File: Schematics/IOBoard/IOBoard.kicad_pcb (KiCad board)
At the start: 2 copper layers, 46.9 x 12.1 mm, 8 parts, among them J1 OLED, J2 Mainboard, J3 Main_output, U1 ATSAMD21E18A-M

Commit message: IOBoard completed
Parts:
- removed C/D: SW(C/D), Connector_PinHeader_2.54mm:PinHeader_1x02_P2.54mm_Vertical
- removed R6: 10k, Resistor_SMD:R_0603_1608Metric
- added C2: 10uF, Capacitor_SMD:C_0603_1608Metric, F.Cu at (111.4, 67.7)
- added J4: MainBoard, Connector_PinSocket_2.54mm:PinSocket_2x05_P2.54mm_Vertical_SMD, B.Cu at (114.3, 63.7)
- added JP1: D0, Jumper:SolderJumper-3_P1.3mm_Bridged12_Pad1.0x1.5mm, F.Cu at (105.8, 67.1)
- added JP2: D1, Jumper:SolderJumper-3_P1.3mm_Bridged12_Pad1.0x1.5mm, F.Cu at (108.5, 67.1)
- added JP3: D1, Jumper:SolderJumper-3_P1.3mm_Bridged12_Pad1.0x1.5mm, B.Cu at (129.8, 60.6)
- added R2: 10k, Resistor_SMD:R_0603_1608Metric, F.Cu at (118.2, 60.3)
- J2: value Mainboard -> Prog; footprint Connector_PinHeader_2.54mm:PinHeader_2x06_P2.54mm_Vertical_SMD -> Connector:Tag-Connect_TC2030-IDC-NL_2x03_P1.27mm_Vertical
- moved J2 11.6 mm to (125.9, 63.7)
- moved C1 5.76 mm to (115.3, 59.4)
- turned U1 to 0 degrees
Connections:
- net /I2C_SDA_IN renamed /TX
- J1 pad 3: /I2C_SCL_OUT -> /OLED_SCL_I2C
- J1 pad 4: /I2C_SDA_OUT -> /OLED_SDA_I2C
- J2 pad 1: GND -> /SWD
- J2 pad 2: /SEL3 -> /SWC
- J2 pad 3: /SEL2 -> GND
- J2 pad 4: /SEL1 -> /RX
- J2 pad 5: GND -> +3V3
- J3 pad 1: /DAC/ADC/1-Wire -> /OUTPUT
- U1 pad 1: Net-(D1-Pad1) -> /OLED_SDA_I2C
- U1 pad 11: /I2C_SDA_OUT -> /D1_I2C
- U1 pad 12: /I2C_SCL_OUT -> /D0_I2C
- U1 pad 13: (no net) -> Net-(D1-Pad2)
- U1 pad 14: (no net) -> Net-(D1-Pad1)
- U1 pad 15: /SEL2 -> (no net)
- U1 pad 16: /SEL1 -> (no net)
- U1 pad 17: /SEL3 -> /TX/RX
- U1 pad 18: (no net) -> /SEL0
- U1 pad 19: (no net) -> /SEL1
- U1 pad 2: Net-(D1-Pad2) -> /OLED_SCL_I2C
- U1 pad 20: (no net) -> /SEL2
- U1 pad 22: /I2C_SCL_IN -> /RX
- U1 pad 23: /USB_D+ -> (no net)
- U1 pad 24: /USB_D- -> (no net)
- U1 pad 3: (no net) -> /DAC/ADC
- U1 pad 4: /DAC/ADC/1-Wire -> (no net)
- U1 pad 5: (no net) -> /D0_SPI
- U1 pad 6: (no net) -> /SCK
- U1 pad 7: (no net) -> /SS
- U1 pad 8: (no net) -> /D1_SPI
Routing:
- net /I2C_SDA_OUT: track 28.2 -> 0.00 mm
- net /DAC/ADC: track 0.00 -> 24.7 mm, vias 0 -> 1
- net /OLED_SCL_I2C: track 0.00 -> 24.7 mm
- net /DAC/ADC/1-Wire: track 22.3 -> 0.00 mm
- net /I2C_SCL_OUT: track 21.4 -> 0.00 mm
- net /OLED_SDA_I2C: track 0.00 -> 20.0 mm
- net /TX/RX: track 0.00 -> 19.9 mm, vias 0 -> 1
- net GND: track 36.6 -> 55.3 mm, vias 6 -> 5
- net /D0_I2C: track 0.00 -> 12.3 mm
- net /USB_D+: track 12.2 -> 0.00 mm, vias 1 -> 0
- net /SWD: track 11.5 -> 21.3 mm, vias 0 -> 1
- net /SWC: track 8.80 -> 17.8 mm, vias 0 -> 1
- net /RX: track 0.00 -> 8.78 mm, vias 0 -> 1
- net /D1_I2C: track 0.00 -> 8.70 mm
- net /D1: track 0.00 -> 7.76 mm, vias 0 -> 1
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
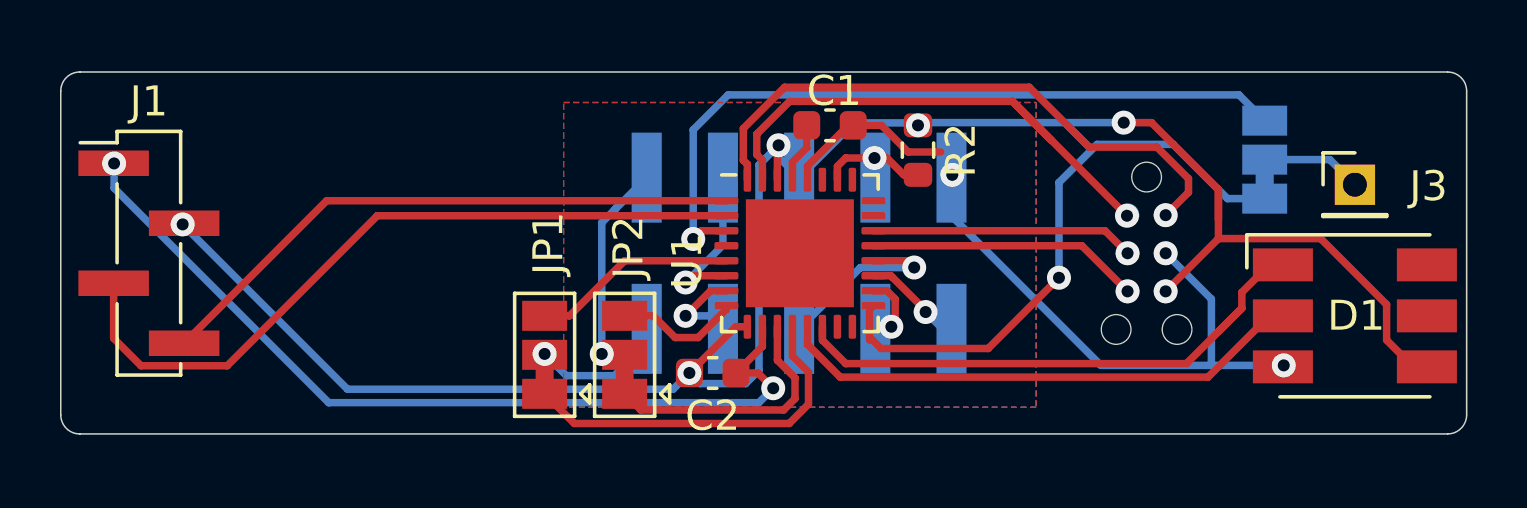
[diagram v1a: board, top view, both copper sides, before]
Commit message: Finished circuit - pre mousebites
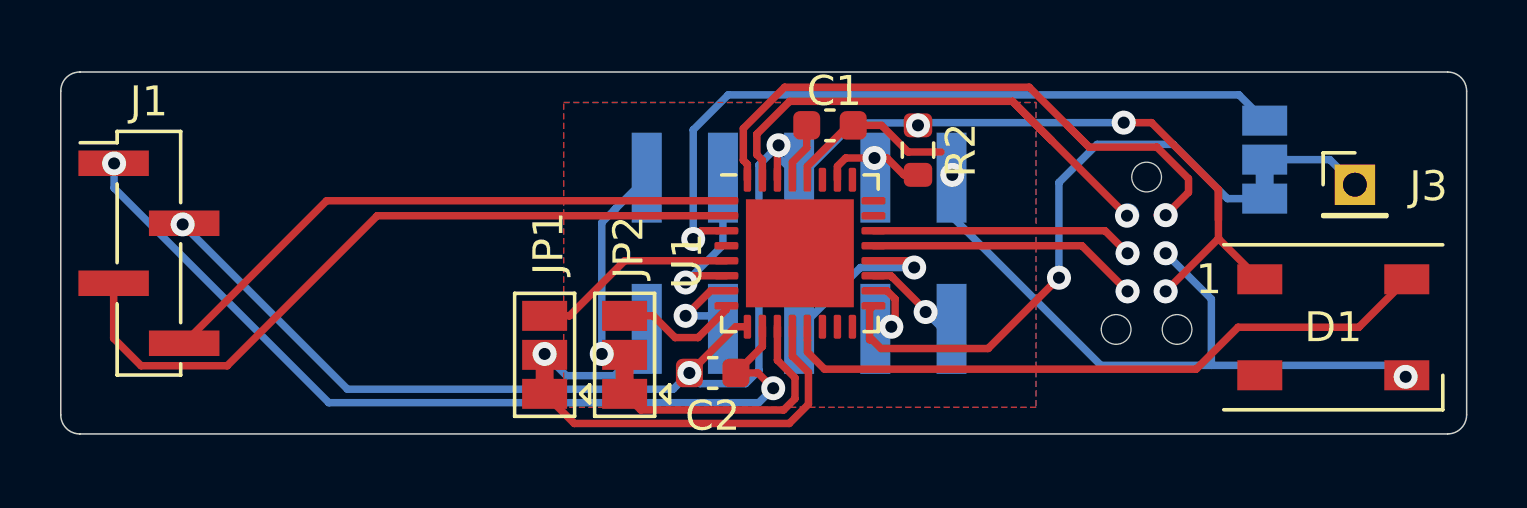
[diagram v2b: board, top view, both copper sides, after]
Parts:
- D1: value APA102 -> WS2812B; footprint LED_SMD:LED_RGB_5050-6 -> LED_SMD:LED_WS2812B_PLCC4_5.0x5.0mm_P3.2mm
- moved D1 0.81 mm to (132.1, 66.2)
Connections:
- D1 pad 1: Net-(D1-Pad1) -> +3V3
- D1 pad 2: Net-(D1-Pad2) -> (no net)
- D1 pad 4: +3V3 -> Net-(U1-Pad13)
- U1 pad 13: Net-(D1-Pad2) -> Net-(U1-Pad13)
- U1 pad 14: Net-(D1-Pad1) -> (no net)
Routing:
- net Net-(U1-Pad13): track 0.00 -> 22.3 mm
- net Net-(D1-Pad1): track 19.3 -> 0.00 mm
- net Net-(D1-Pad2): track 17.7 -> 0.00 mm
- net +3V3: track 65.3 -> 57.8 mm
- net GND: track 55.3 -> 60.5 mm
